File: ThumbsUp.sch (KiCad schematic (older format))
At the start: 159 parts, among them IC1 RP2040, IC2 W25Q128JVSIM, J1 Conn_01x04_Male, J10 Raiser_Male, J11 Raiser_Female, J12 Raiser_Male, J13 Raiser_Female, J14 Raiser_Male, J15 Raiser_Female, J16 Raiser_Male, J17 Raiser_Female, J18 Raiser_Male, J19 52559-1233, J2 Conn_01x04_Male, J20 Conn_01x04_Female, J21 Conn_01x04_Female, J22 Conn_01x04_Female, J23 Conn_01x04_Female, J24 Conn_01x04_Male, J25 Conn_01x04_Male, J26 Conn_01x04_Male, J27 Conn_01x04_Male, J28 Conn_01x04_Female, J29 Conn_01x04_Female, J3 Conn_01x04_Female, J30 Conn_01x04_Female, J31 Conn_01x04_Female, J32 USB_C_Receptacle_USB2.0, J4 Conn_01x04_Male, J5 Conn_01x04_Female, J6 Conn_01x04_Male, J7 Conn_01x04_Male, J8 Conn_01x04_Male, J9 Raiser_Female, U1 NCP1117-3.3_SOT223, Y1 ABLS-12.000MHZ-B4-T

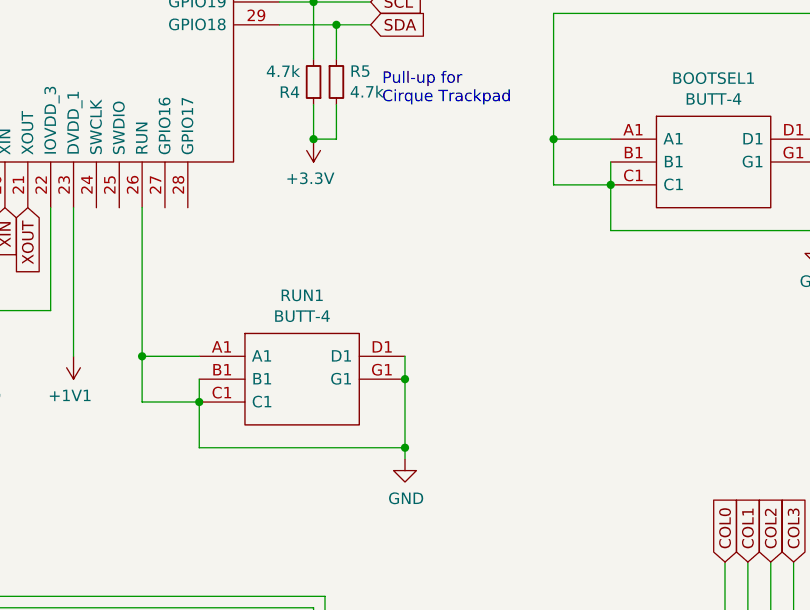
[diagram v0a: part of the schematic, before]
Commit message: Traced bottom PCB.
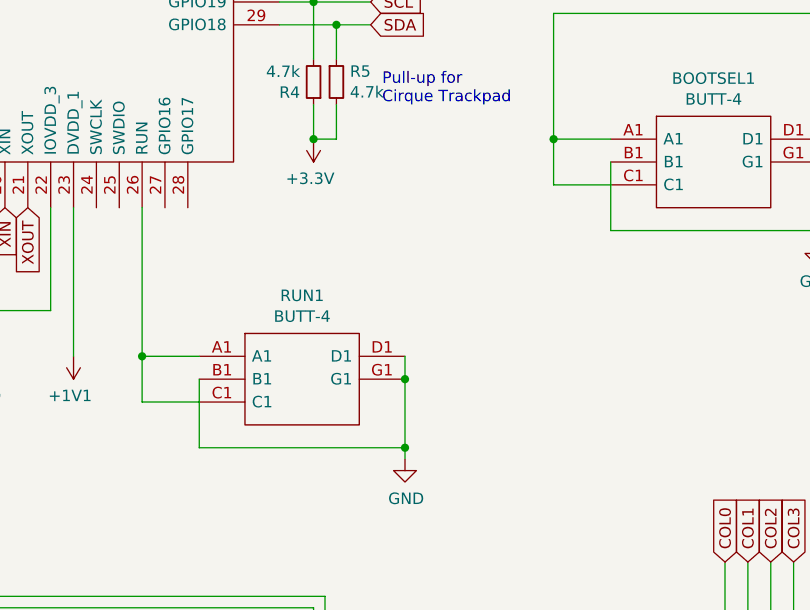
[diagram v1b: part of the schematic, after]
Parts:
- MX1, MX10, MX11, MX12, MX13, MX14, MX15, MX16, MX17, MX18, MX19, MX2, MX20, MX21, MX22, MX23, MX24, MX25, MX26, MX27, MX28, MX29, MX3, MX30, MX31, MX32, MX33, MX34, MX35, MX36, MX37, MX38, MX39, MX4, MX40, MX41, MX42, MX43, MX44, MX45, MX46, MX5, MX6, MX7, MX8, MX9: footprint keyswitches:Kailh_socket_PG1350_optional -> keyswitches:Kailh_socket_PG1350
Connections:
- net GND: no longer BOOTSEL1.A1, BOOTSEL1.C1, IC1.26 (RUN), R3.1, RUN1.A1, RUN1.C1
- new net: BOOTSEL1.A1, BOOTSEL1.C1, R3.1
- new net: IC1.26 (RUN), RUN1.A1, RUN1.C1

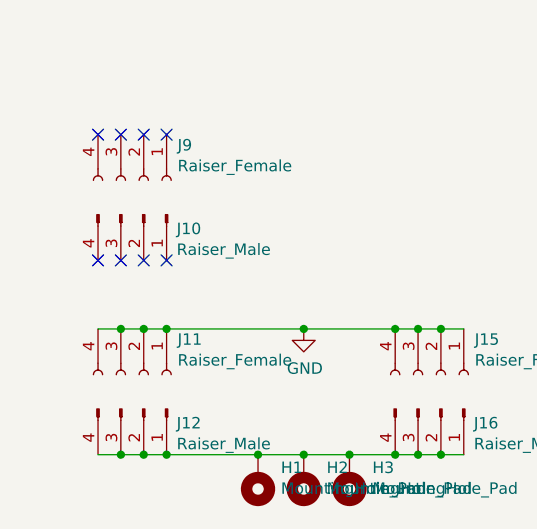
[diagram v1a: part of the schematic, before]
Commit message: Traced middle PCB.
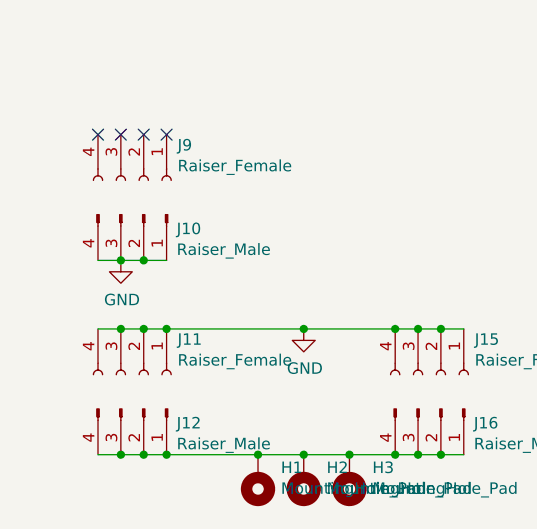
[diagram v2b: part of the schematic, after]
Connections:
- net GND: now also J10.1 (Pin_1), J10.2 (Pin_2), J10.3 (Pin_3), J10.4 (Pin_4)
- no-connect marks 22 -> 18
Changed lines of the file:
@@
 NoConn ~ 1750 11350
 NoConn ~ 1850 11350
-NoConn ~ 1550 11900
-NoConn ~ 1650 11900
-NoConn ~ 1750 11900
-NoConn ~ 1850 11900
 $Comp
 L Connector:Conn_01x04_Female J17
@@
 Wire Wire Line
 	5500 4450 5500 4750
+Wire Wire Line
+	1850 11900 1750 11900
+Connection ~ 1650 11900
+Wire Wire Line
+	1650 11900 1550 11900
+Connection ~ 1750 11900
+Wire Wire Line
+	1750 11900 1650 11900
+$Comp
+L power:GND #PWR?
+U 1 1 664356B7
+P 1650 11900
+F 0 "#PWR?" H 1650 11650 50  0001 C CNN
+F 1 "GND" H 1655 11727 50  0000 C CNN
+F 2 "" H 1650 11900 50  0001 C CNN
+F 3 "" H 1650 11900 50  0001 C CNN
+	1    1650 11900
+	1    0    0    -1
+$EndComp
 $EndSCHEMATC
